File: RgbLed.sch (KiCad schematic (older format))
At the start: 7 parts, among them Q1 BC817, Q2 BC817, Q3 BC817

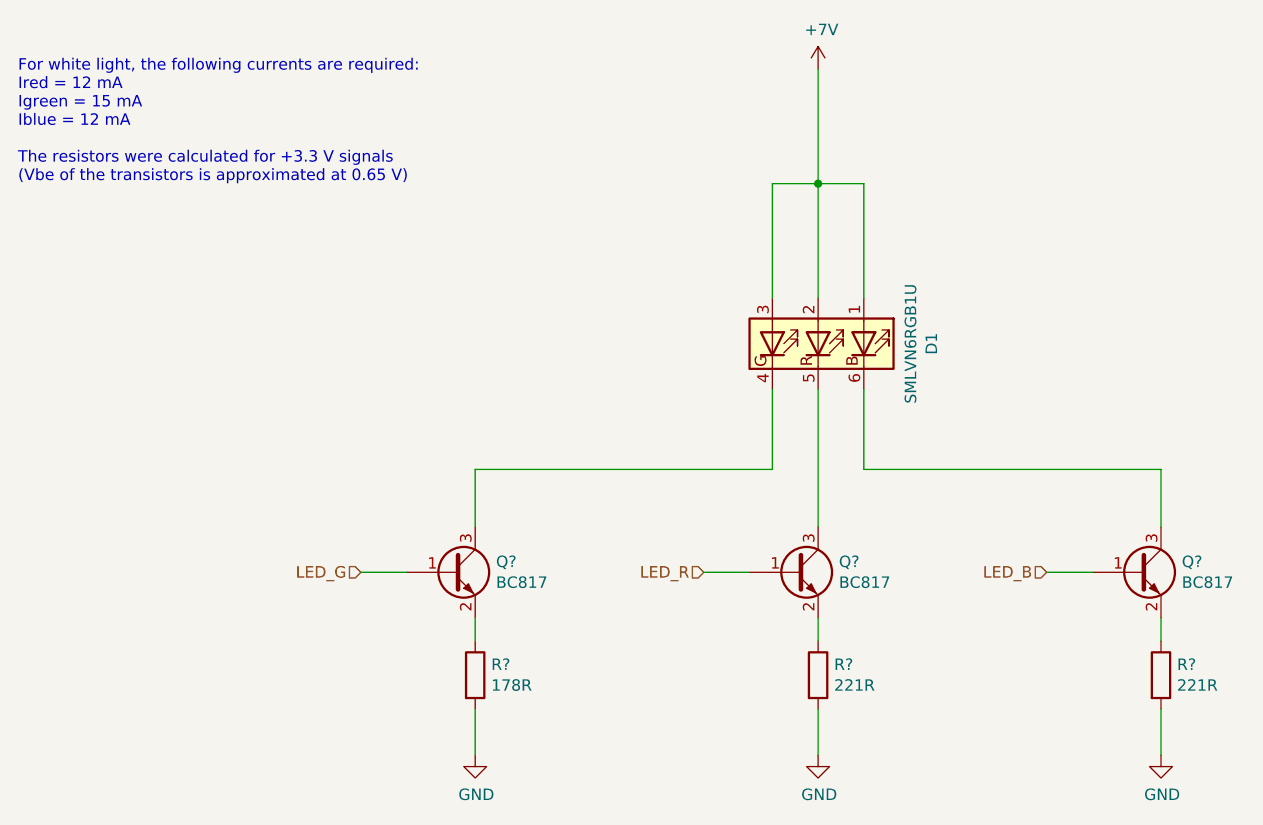
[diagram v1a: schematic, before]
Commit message: Add the power supply and motor driver ICs
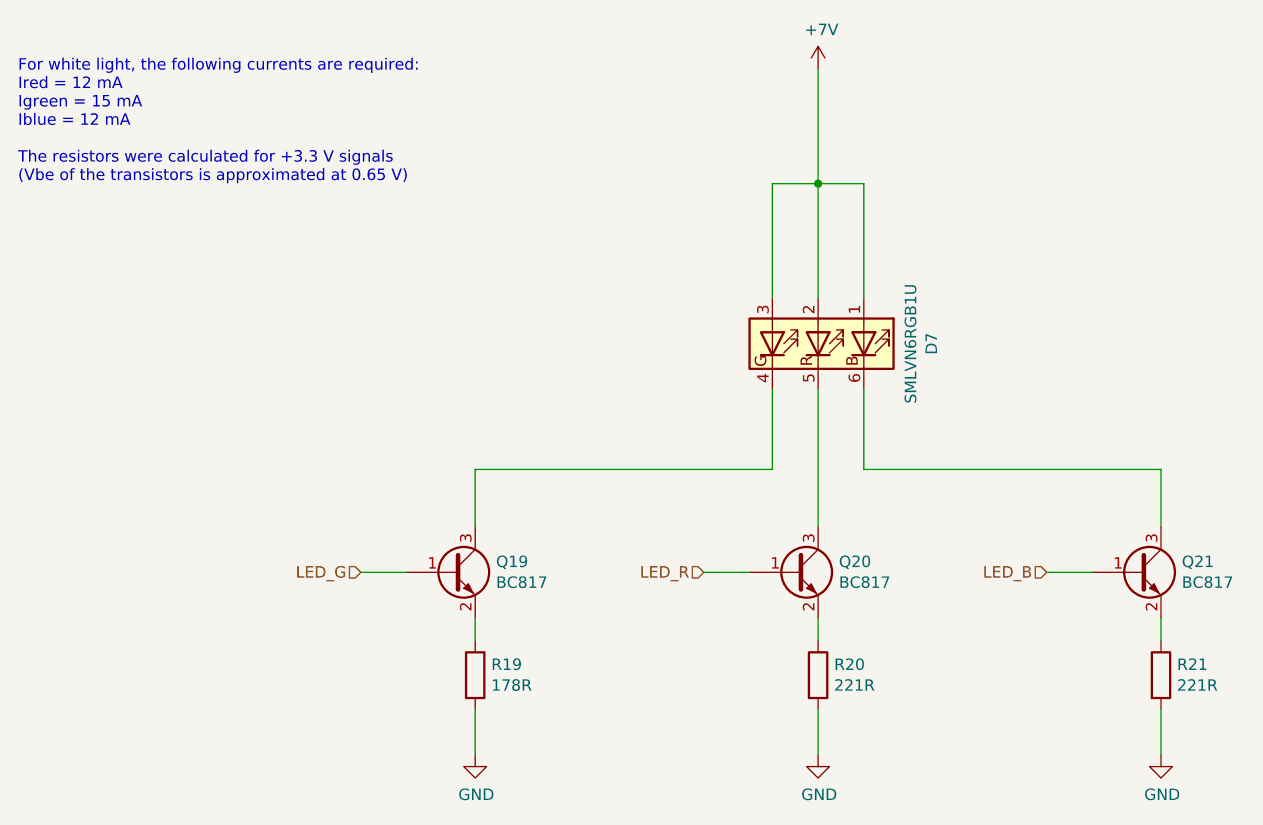
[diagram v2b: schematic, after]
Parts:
- D1: Part_Number (none) -> SMLVN6RGB1U1
- Q1, Q2, Q3: Part_Number (none) -> BC817-25,215
- R1: Part_Number (none) -> CR0603-FX-1780ELF
- R2, R3: Part_Number (none) -> CR0603-FX-2210ELF

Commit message: Add the MPM54304 footprint
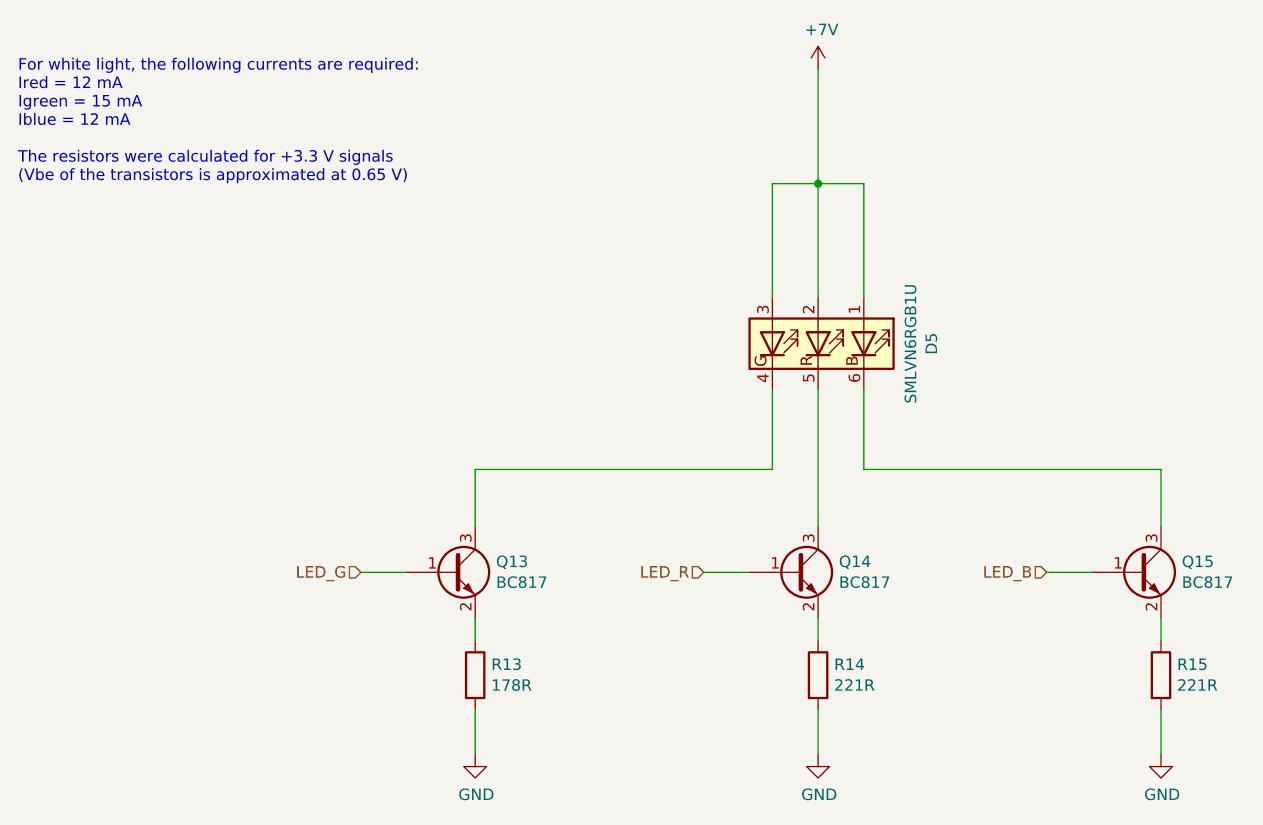
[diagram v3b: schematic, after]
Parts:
- D1: footprint LED_SMD:LED_ROHM_SMLVN6 -> LitterRobot:ROHM_SMLVN6
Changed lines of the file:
@@
 $Descr A4 11693 8268
 encoding utf-8
-Sheet 6 16
+Sheet 7 16
 Title "Litter Robot 3 - RGB LED"
 Date "2021-02-28"
@@
 AR Path="/603E03AA/603BFBE6/603E2469" Ref="Q?"  Part="1"
 AR Path="/603E03AA/603BFD93/603E2469" Ref="Q19"  Part="1"
-F 0 "Q19" H 4091 4246 50  0000 L CNN
+F 0 "Q13" H 4091 4246 50  0000 L CNN
 F 1 "BC817" H 4091 4155 50  0000 L CNN
 F 2 "Package_TO_SOT_SMD:SOT-23" H 4100 4125 50  0001 L CIN
@@
 AR Path="/603E03AA/603BFBE6/603E246F" Ref="R?"  Part="1"
 AR Path="/603E03AA/603BFD93/603E246F" Ref="R19"  Part="1"
-F 0 "R19" H 4070 4696 50  0000 L CNN
+F 0 "R13" H 4070 4696 50  0000 L CNN
 F 1 "178R" H 4070 4605 50  0000 L CNN
 F 2 "Resistor_SMD:R_0603_1608Metric" V 3930 4650 50  0001 C CNN
@@
 AR Path="/603E03AA/603BFBE6/603E7162" Ref="D?"  Part="1"
 AR Path="/603E03AA/603BFD93/603E7162" Ref="D7"  Part="1"
-F 0 "D7" H 5500 3697 50  0000 C CNN
+F 0 "D5" H 5500 3697 50  0000 C CNN
 F 1 "SMLVN6RGB1U" H 5500 3606 50  0000 C CNN
-F 2 "LED_SMD:LED_ROHM_SMLVN6" H 5500 2850 50  0001 C CNN
+F 2 "LitterRobot:ROHM_SMLVN6" H 5500 2850 50  0001 C CNN
 F 3 "https://fscdn.rohm.com/en/products/databook/datasheet/opto/led/chip_multi/smlvn6rgb1w-e.pdf" H 5500 3150 50  0001 C CNN
 F 4 "SMLVN6RGB1U1" H 5500 3200 50  0001 C CNN "Part_Number"
@@
 AR Path="/603E03AA/603BFBE6/603FCE1E" Ref="R?"  Part="1"
 AR Path="/603E03AA/603BFD93/603FCE1E" Ref="R20"  Part="1"
-F 0 "R20" H 5570 4696 50  0000 L CNN
+F 0 "R14" H 5570 4696 50  0000 L CNN
 F 1 "221R" H 5570 4605 50  0000 L CNN
 F 2 "Resistor_SMD:R_0603_1608Metric" V 5430 4650 50  0001 C CNN
@@
 AR Path="/603E03AA/603BFBE6/603FDBA6" Ref="R?"  Part="1"
 AR Path="/603E03AA/603BFD93/603FDBA6" Ref="R21"  Part="1"
-F 0 "R21" H 7070 4696 50  0000 L CNN
+F 0 "R15" H 7070 4696 50  0000 L CNN
 F 1 "221R" H 7070 4605 50  0000 L CNN
 F 2 "Resistor_SMD:R_0603_1608Metric" V 6930 4650 50  0001 C CNN
@@
 AR Path="/603E03AA/603BFBE6/603FDE8C" Ref="#PWR?"  Part="1"
 AR Path="/603E03AA/603BFD93/603FDE8C" Ref="#PWR033"  Part="1"
-F 0 "#PWR033" H 4000 4750 50  0001 C CNN
+F 0 "#PWR025" H 4000 4750 50  0001 C CNN
 F 1 "GND" H 4005 4827 50  0000 C CNN
 F 2 "" H 4000 5000 50  0001 C CNN
@@
 AR Path="/603E03AA/603BFBE6/603FF30B" Ref="#PWR?"  Part="1"
 AR Path="/603E03AA/603BFD93/603FF30B" Ref="#PWR035"  Part="1"
-F 0 "#PWR035" H 5500 4750 50  0001 C CNN
+F 0 "#PWR027" H 5500 4750 50  0001 C CNN
 F 1 "GND" H 5505 4827 50  0000 C CNN
 F 2 "" H 5500 5000 50  0001 C CNN
@@
 AR Path="/603E03AA/603BFBE6/603FF5B6" Ref="#PWR?"  Part="1"
 AR Path="/603E03AA/603BFD93/603FF5B6" Ref="#PWR036"  Part="1"
-F 0 "#PWR036" H 7000 4750 50  0001 C CNN
+F 0 "#PWR028" H 7000 4750 50  0001 C CNN
 F 1 "GND" H 7005 4827 50  0000 C CNN
 F 2 "" H 7000 5000 50  0001 C CNN
@@
 AR Path="/603E03AA/603BFBE6/60414150" Ref="#PWR?"  Part="1"
 AR Path="/603E03AA/603BFD93/60414150" Ref="#PWR034"  Part="1"
-F 0 "#PWR034" H 5500 1850 50  0001 C CNN
+F 0 "#PWR026" H 5500 1850 50  0001 C CNN
 F 1 "+7V" H 5515 2173 50  0000 C CNN
 F 2 "" H 5500 2000 50  0001 C CNN
@@
 AR Path="/603E03AA/603BFBE6/6045060B" Ref="Q?"  Part="1"
 AR Path="/603E03AA/603BFD93/6045060B" Ref="Q20"  Part="1"
-F 0 "Q20" H 5591 4246 50  0000 L CNN
+F 0 "Q14" H 5591 4246 50  0000 L CNN
 F 1 "BC817" H 5591 4155 50  0000 L CNN
 F 2 "Package_TO_SOT_SMD:SOT-23" H 5600 4125 50  0001 L CIN
@@
 AR Path="/603E03AA/603BFBE6/60450E24" Ref="Q?"  Part="1"
 AR Path="/603E03AA/603BFD93/60450E24" Ref="Q21"  Part="1"
-F 0 "Q21" H 7091 4246 50  0000 L CNN
+F 0 "Q15" H 7091 4246 50  0000 L CNN
 F 1 "BC817" H 7091 4155 50  0000 L CNN
 F 2 "Package_TO_SOT_SMD:SOT-23" H 7100 4125 50  0001 L CIN

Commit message: Add the push buttons and mounting holes
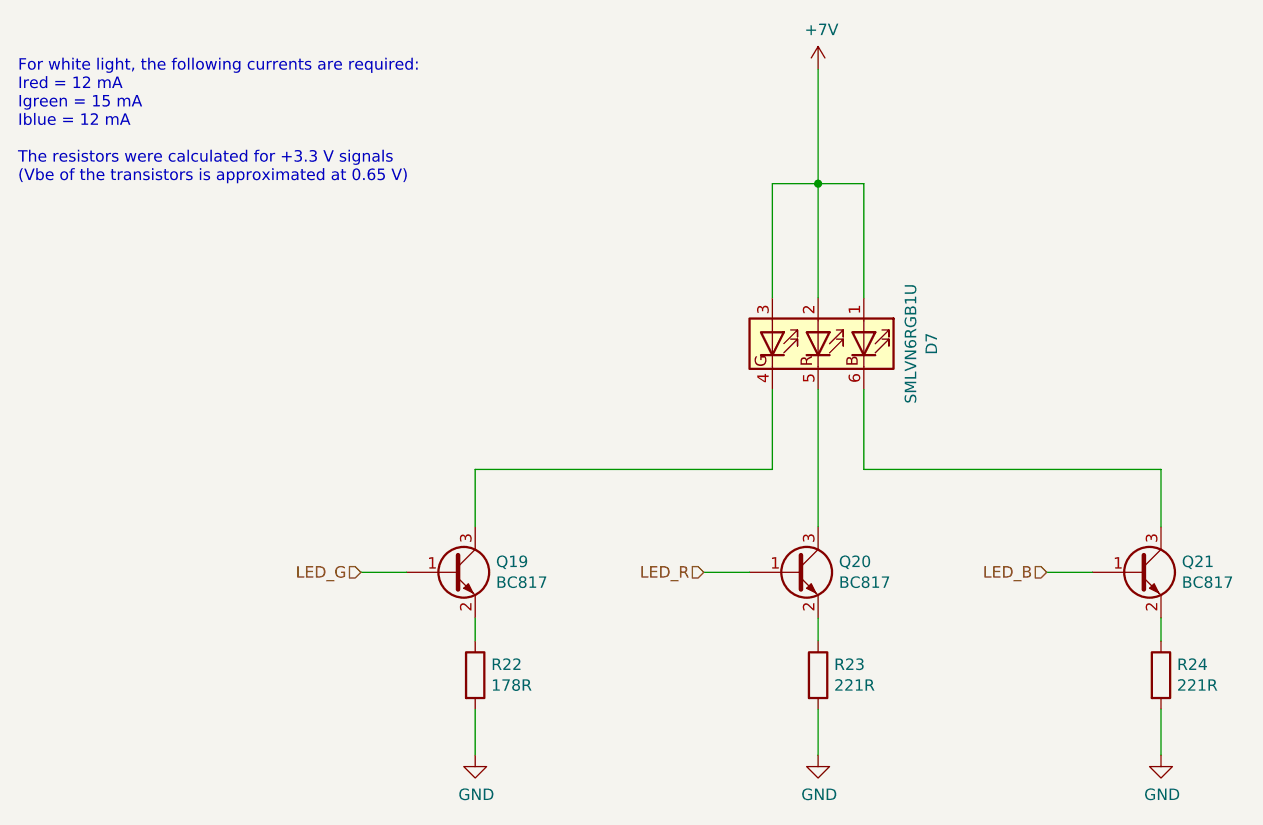
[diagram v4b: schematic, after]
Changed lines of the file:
@@
 AR Path="/603E03AA/603BFBE6/603E2469" Ref="Q?"  Part="1"
 AR Path="/603E03AA/603BFD93/603E2469" Ref="Q19"  Part="1"
-F 0 "Q13" H 4091 4246 50  0000 L CNN
+F 0 "Q19" H 4091 4246 50  0000 L CNN
 F 1 "BC817" H 4091 4155 50  0000 L CNN
 F 2 "Package_TO_SOT_SMD:SOT-23" H 4100 4125 50  0001 L CIN
@@
 AR Path="/603E03AA/603BFBE1/603E246F" Ref="R?"  Part="1"
 AR Path="/603E03AA/603BFBE6/603E246F" Ref="R?"  Part="1"
-AR Path="/603E03AA/603BFD93/603E246F" Ref="R19"  Part="1"
-F 0 "R13" H 4070 4696 50  0000 L CNN
+AR Path="/603E03AA/603BFD93/603E246F" Ref="R22"  Part="1"
+F 0 "R22" H 4070 4696 50  0000 L CNN
 F 1 "178R" H 4070 4605 50  0000 L CNN
 F 2 "Resistor_SMD:R_0603_1608Metric" V 3930 4650 50  0001 C CNN
@@
 AR Path="/603E03AA/603BFBE6/603E7162" Ref="D?"  Part="1"
 AR Path="/603E03AA/603BFD93/603E7162" Ref="D7"  Part="1"
-F 0 "D5" H 5500 3697 50  0000 C CNN
+F 0 "D7" H 5500 3697 50  0000 C CNN
 F 1 "SMLVN6RGB1U" H 5500 3606 50  0000 C CNN
 F 2 "LitterRobot:ROHM_SMLVN6" H 5500 2850 50  0001 C CNN
@@
 AR Path="/603E03AA/603BFBE1/603FCE1E" Ref="R?"  Part="1"
 AR Path="/603E03AA/603BFBE6/603FCE1E" Ref="R?"  Part="1"
-AR Path="/603E03AA/603BFD93/603FCE1E" Ref="R20"  Part="1"
-F 0 "R14" H 5570 4696 50  0000 L CNN
+AR Path="/603E03AA/603BFD93/603FCE1E" Ref="R23"  Part="1"
+F 0 "R23" H 5570 4696 50  0000 L CNN
 F 1 "221R" H 5570 4605 50  0000 L CNN
 F 2 "Resistor_SMD:R_0603_1608Metric" V 5430 4650 50  0001 C CNN
@@
 AR Path="/603E03AA/603BFBE1/603FDBA6" Ref="R?"  Part="1"
 AR Path="/603E03AA/603BFBE6/603FDBA6" Ref="R?"  Part="1"
-AR Path="/603E03AA/603BFD93/603FDBA6" Ref="R21"  Part="1"
-F 0 "R15" H 7070 4696 50  0000 L CNN
+AR Path="/603E03AA/603BFD93/603FDBA6" Ref="R24"  Part="1"
+F 0 "R24" H 7070 4696 50  0000 L CNN
 F 1 "221R" H 7070 4605 50  0000 L CNN
 F 2 "Resistor_SMD:R_0603_1608Metric" V 6930 4650 50  0001 C CNN
@@
 AR Path="/603E03AA/603BFBE1/603FDE8C" Ref="#PWR?"  Part="1"
 AR Path="/603E03AA/603BFBE6/603FDE8C" Ref="#PWR?"  Part="1"
-AR Path="/603E03AA/603BFD93/603FDE8C" Ref="#PWR033"  Part="1"
-F 0 "#PWR025" H 4000 4750 50  0001 C CNN
+AR Path="/603E03AA/603BFD93/603FDE8C" Ref="#PWR039"  Part="1"
+F 0 "#PWR039" H 4000 4750 50  0001 C CNN
 F 1 "GND" H 4005 4827 50  0000 C CNN
 F 2 "" H 4000 5000 50  0001 C CNN
@@
 AR Path="/603E03AA/603BFBE1/603FF30B" Ref="#PWR?"  Part="1"
 AR Path="/603E03AA/603BFBE6/603FF30B" Ref="#PWR?"  Part="1"
-AR Path="/603E03AA/603BFD93/603FF30B" Ref="#PWR035"  Part="1"
-F 0 "#PWR027" H 5500 4750 50  0001 C CNN
+AR Path="/603E03AA/603BFD93/603FF30B" Ref="#PWR041"  Part="1"
+F 0 "#PWR041" H 5500 4750 50  0001 C CNN
 F 1 "GND" H 5505 4827 50  0000 C CNN
 F 2 "" H 5500 5000 50  0001 C CNN
@@
 AR Path="/603E03AA/603BFBE1/603FF5B6" Ref="#PWR?"  Part="1"
 AR Path="/603E03AA/603BFBE6/603FF5B6" Ref="#PWR?"  Part="1"
-AR Path="/603E03AA/603BFD93/603FF5B6" Ref="#PWR036"  Part="1"
-F 0 "#PWR028" H 7000 4750 50  0001 C CNN
+AR Path="/603E03AA/603BFD93/603FF5B6" Ref="#PWR042"  Part="1"
+F 0 "#PWR042" H 7000 4750 50  0001 C CNN
 F 1 "GND" H 7005 4827 50  0000 C CNN
 F 2 "" H 7000 5000 50  0001 C CNN
@@
 AR Path="/603E03AA/603BFBE1/60414150" Ref="#PWR?"  Part="1"
 AR Path="/603E03AA/603BFBE6/60414150" Ref="#PWR?"  Part="1"
-AR Path="/603E03AA/603BFD93/60414150" Ref="#PWR034"  Part="1"
-F 0 "#PWR026" H 5500 1850 50  0001 C CNN
+AR Path="/603E03AA/603BFD93/60414150" Ref="#PWR040"  Part="1"
+F 0 "#PWR040" H 5500 1850 50  0001 C CNN
 F 1 "+7V" H 5515 2173 50  0000 C CNN
 F 2 "" H 5500 2000 50  0001 C CNN
@@
 AR Path="/603E03AA/603BFBE6/6045060B" Ref="Q?"  Part="1"
 AR Path="/603E03AA/603BFD93/6045060B" Ref="Q20"  Part="1"
-F 0 "Q14" H 5591 4246 50  0000 L CNN
+F 0 "Q20" H 5591 4246 50  0000 L CNN
 F 1 "BC817" H 5591 4155 50  0000 L CNN
 F 2 "Package_TO_SOT_SMD:SOT-23" H 5600 4125 50  0001 L CIN
@@
 AR Path="/603E03AA/603BFBE6/60450E24" Ref="Q?"  Part="1"
 AR Path="/603E03AA/603BFD93/60450E24" Ref="Q21"  Part="1"
-F 0 "Q15" H 7091 4246 50  0000 L CNN
+F 0 "Q21" H 7091 4246 50  0000 L CNN
 F 1 "BC817" H 7091 4155 50  0000 L CNN
 F 2 "Package_TO_SOT_SMD:SOT-23" H 7100 4125 50  0001 L CIN

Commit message: Place the main components on the PCB
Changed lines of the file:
@@
 $Descr A4 11693 8268
 encoding utf-8
-Sheet 7 16
+Sheet 4 16
 Title "Litter Robot 3 - RGB LED"
 Date "2021-02-28"
@@
 AR Path="/603E03AA/603BFBE6/603E2469" Ref="Q?"  Part="1"
 AR Path="/603E03AA/603BFD93/603E2469" Ref="Q19"  Part="1"
-F 0 "Q19" H 4091 4246 50  0000 L CNN
+F 0 "Q4" H 4091 4246 50  0000 L CNN
 F 1 "BC817" H 4091 4155 50  0000 L CNN
 F 2 "Package_TO_SOT_SMD:SOT-23" H 4100 4125 50  0001 L CIN
@@
 AR Path="/603E03AA/603BFBE6/603E246F" Ref="R?"  Part="1"
 AR Path="/603E03AA/603BFD93/603E246F" Ref="R22"  Part="1"
-F 0 "R22" H 4070 4696 50  0000 L CNN
+F 0 "R4" H 4070 4696 50  0000 L CNN
 F 1 "178R" H 4070 4605 50  0000 L CNN
 F 2 "Resistor_SMD:R_0603_1608Metric" V 3930 4650 50  0001 C CNN
@@
 AR Path="/603E03AA/603BFBE6/603E7162" Ref="D?"  Part="1"
 AR Path="/603E03AA/603BFD93/603E7162" Ref="D7"  Part="1"
-F 0 "D7" H 5500 3697 50  0000 C CNN
+F 0 "D2" H 5500 3697 50  0000 C CNN
 F 1 "SMLVN6RGB1U" H 5500 3606 50  0000 C CNN
 F 2 "LitterRobot:ROHM_SMLVN6" H 5500 2850 50  0001 C CNN
@@
 AR Path="/603E03AA/603BFBE6/603FCE1E" Ref="R?"  Part="1"
 AR Path="/603E03AA/603BFD93/603FCE1E" Ref="R23"  Part="1"
-F 0 "R23" H 5570 4696 50  0000 L CNN
+F 0 "R5" H 5570 4696 50  0000 L CNN
 F 1 "221R" H 5570 4605 50  0000 L CNN
 F 2 "Resistor_SMD:R_0603_1608Metric" V 5430 4650 50  0001 C CNN
@@
 AR Path="/603E03AA/603BFBE6/603FDBA6" Ref="R?"  Part="1"
 AR Path="/603E03AA/603BFD93/603FDBA6" Ref="R24"  Part="1"
-F 0 "R24" H 7070 4696 50  0000 L CNN
+F 0 "R6" H 7070 4696 50  0000 L CNN
 F 1 "221R" H 7070 4605 50  0000 L CNN
 F 2 "Resistor_SMD:R_0603_1608Metric" V 6930 4650 50  0001 C CNN
@@
 AR Path="/603E03AA/603BFBE6/6045060B" Ref="Q?"  Part="1"
 AR Path="/603E03AA/603BFD93/6045060B" Ref="Q20"  Part="1"
-F 0 "Q20" H 5591 4246 50  0000 L CNN
+F 0 "Q5" H 5591 4246 50  0000 L CNN
 F 1 "BC817" H 5591 4155 50  0000 L CNN
 F 2 "Package_TO_SOT_SMD:SOT-23" H 5600 4125 50  0001 L CIN
@@
 AR Path="/603E03AA/603BFBE6/60450E24" Ref="Q?"  Part="1"
 AR Path="/603E03AA/603BFD93/60450E24" Ref="Q21"  Part="1"
-F 0 "Q21" H 7091 4246 50  0000 L CNN
+F 0 "Q6" H 7091 4246 50  0000 L CNN
 F 1 "BC817" H 7091 4155 50  0000 L CNN
 F 2 "Package_TO_SOT_SMD:SOT-23" H 7100 4125 50  0001 L CIN
